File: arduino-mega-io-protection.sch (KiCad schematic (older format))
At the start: 34 parts, among them J108 CONN_01X36, J109 CONN_01X10, J110 CONN_02X18, J111 CONN_01X08, J112 CONN_01X08, J113 CONN_01X08, J114 CONN_01X08, J115 CONN_01X08

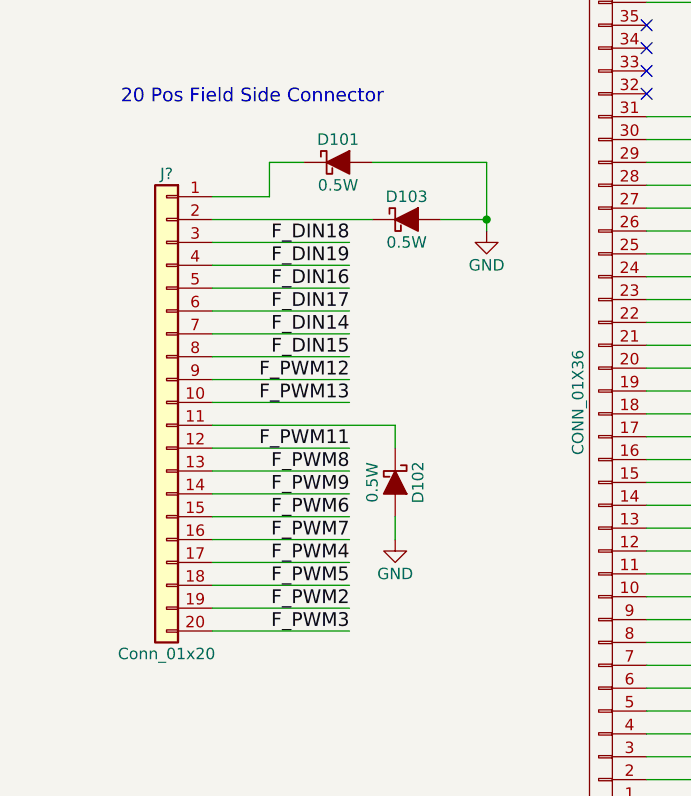
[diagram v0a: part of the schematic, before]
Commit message: updating schematic and library to use a Phoenix header for the 1x20
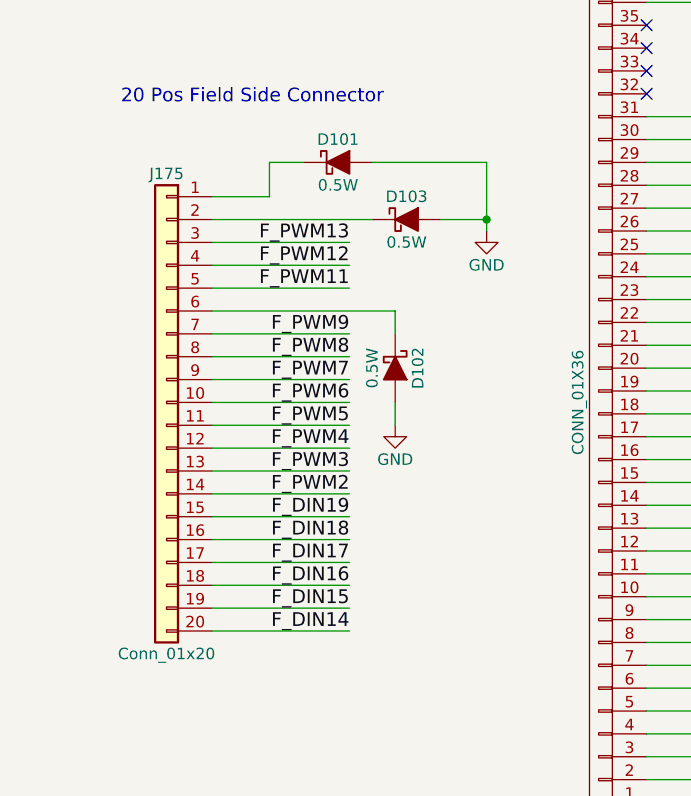
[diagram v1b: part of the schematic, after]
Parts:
- J175: renamed from J?; footprint (none) -> 3ML_Conn_Headers:Phoenix-1x20-1709678; MFN 1709678 -> Phoenix Contact
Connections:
- net F_DIN14: now also J175.20 (Pin_20); no longer J175.7 (Pin_7)
- net F_DIN15: now also J175.19 (Pin_19); no longer J175.8 (Pin_8)
- net F_DIN16: now also J175.18 (Pin_18); no longer J175.5 (Pin_5)
- net F_DIN17: now also J175.17 (Pin_17); no longer J175.6 (Pin_6)
- net F_DIN18: now also J175.16 (Pin_16); no longer J175.3 (Pin_3)
- net F_DIN19: now also J175.15 (Pin_15); no longer J175.4 (Pin_4)
- net F_PWM11: now also J175.5 (Pin_5); no longer J175.12 (Pin_12)
- net F_PWM12: now also J175.4 (Pin_4); no longer J175.9 (Pin_9)
- net F_PWM13: now also J175.3 (Pin_3); no longer J175.10 (Pin_10)
- net F_PWM2: now also J175.14 (Pin_14); no longer J175.19 (Pin_19)
- net F_PWM3: now also J175.13 (Pin_13); no longer J175.20 (Pin_20)
- net F_PWM4: now also J175.12 (Pin_12); no longer J175.17 (Pin_17)
- net F_PWM5: now also J175.11 (Pin_11); no longer J175.18 (Pin_18)
- net F_PWM6: now also J175.10 (Pin_10); no longer J175.15 (Pin_15)
- net F_PWM7: now also J175.9 (Pin_9); no longer J175.16 (Pin_16)
- net F_PWM8: now also J175.8 (Pin_8); no longer J175.13 (Pin_13)
- net F_PWM9: now also J175.7 (Pin_7); no longer J175.14 (Pin_14)
- net at D102.1 (K): now also J175.6 (Pin_6); no longer J175.11 (Pin_11)
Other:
- moved on the sheet: D102
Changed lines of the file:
@@
 Text Label 7800 2550 0    60   ~ 0
 F_PWM13
-Text Label 1950 5250 2    60   ~ 0
+Text Label 1950 4750 2    60   ~ 0
 F_PWM2
-Text Label 1950 5350 2    60   ~ 0
+Text Label 1950 4650 2    60   ~ 0
 F_PWM3
-Text Label 1950 5050 2    60   ~ 0
+Text Label 1950 4550 2    60   ~ 0
 F_PWM4
-Text Label 1950 5150 2    60   ~ 0
+Text Label 1950 4450 2    60   ~ 0
 F_PWM5
-Text Label 1950 4850 2    60   ~ 0
+Text Label 1950 4350 2    60   ~ 0
 F_PWM6
-Text Label 1950 4950 2    60   ~ 0
+Text Label 1950 4250 2    60   ~ 0
 F_PWM7
-Text Label 1950 4650 2    60   ~ 0
+Text Label 1950 4150 2    60   ~ 0
 F_PWM8
-Text Label 1950 4750 2    60   ~ 0
+Text Label 1950 4050 2    60   ~ 0
 F_PWM9
-Text Label 1950 4550 2    60   ~ 0
+Text Label 1950 3850 2    60   ~ 0
 F_PWM11
-Text Label 1950 4250 2    60   ~ 0
+Text Label 1950 3750 2    60   ~ 0
 F_PWM12
-Text Label 1950 4350 2    60   ~ 0
+Text Label 1950 3650 2    60   ~ 0
 F_PWM13
 $Comp
@@
 Text Label 11850 6250 0    60   ~ 0
 DIN19
-Text Label 1950 4050 2    60   ~ 0
+Text Label 1950 5350 2    60   ~ 0
 F_DIN14
-Text Label 1950 4150 2    60   ~ 0
+Text Label 1950 5250 2    60   ~ 0
 F_DIN15
-Text Label 1950 3850 2    60   ~ 0
+Text Label 1950 5150 2    60   ~ 0
 F_DIN16
-Text Label 1950 3950 2    60   ~ 0
+Text Label 1950 5050 2    60   ~ 0
 F_DIN17
-Text Label 1950 3650 2    60   ~ 0
+Text Label 1950 4950 2    60   ~ 0
 F_DIN18
-Text Label 1950 3750 2    60   ~ 0
+Text Label 1950 4850 2    60   ~ 0
 F_DIN19
 Text Label 7800 2400 0    60   ~ 0
@@
 L GND #PWR09
 U 1 1 593C6552
-P 2150 4950
-F 0 "#PWR09" H 2150 4700 50  0001 C CNN
-F 1 "GND" H 2150 4800 50  0000 C CNN
-F 2 "" H 2150 4950 50  0001 C CNN
-F 3 "" H 2150 4950 50  0001 C CNN
-	1    2150 4950
+P 2150 4450
+F 0 "#PWR09" H 2150 4200 50  0001 C CNN
+F 1 "GND" H 2150 4300 50  0000 C CNN
+F 2 "" H 2150 4450 50  0001 C CNN
+F 3 "" H 2150 4450 50  0001 C CNN
+	1    2150 4450
 	1    0    0    -1
 $EndComp
@@
 L D_Schottky_ALT D102
 U 1 1 598AE553
-P 2150 4700
-F 0 "D102" H 2150 4800 50  0000 C CNN
-F 1 "0.5W" H 2150 4600 50  0000 C CNN
-F 2 "Diodes_SMD:SOD-123" H 2150 4700 50  0001 C CNN
-F 3 "http://www.mccsemi.com/up_pdf/MBR0520~MBR0580(SOD123).pdf" H 2150 4700 50  0001 C CNN
-F 4 "X" H 2150 4700 60  0001 C CNN "Characteristics"
-F 5 "DIODE SCHOTTKY 80V 500MA SOD123" H 2150 4700 60  0001 C CNN "Description"
-F 6 "Micro Commercial Co" H 2150 4700 60  0001 C CNN "MFN"
-F 7 "SOD-123" H 2150 4700 60  0001 C CNN "Package ID"
-F 8 "Digikey" H 2150 4700 60  0001 C CNN "Source"
-F 9 "Y" H 2150 4700 60  0001 C CNN "Critical"
-F 10 "X" H 2150 4700 60  0001 C CNN "Notes"
-F 11 "1" H 2150 4700 60  0001 C CNN "Populate"
-F 12 "MBR0580-TP" H 2150 4700 60  0001 C CNN "MPN"
-	1    2150 4700
+P 2150 4200
+F 0 "D102" H 2150 4300 50  0000 C CNN
+F 1 "0.5W" H 2150 4100 50  0000 C CNN
+F 2 "Diodes_SMD:SOD-123" H 2150 4200 50  0001 C CNN
+F 3 "http://www.mccsemi.com/up_pdf/MBR0520~MBR0580(SOD123).pdf" H 2150 4200 50  0001 C CNN
+F 4 "X" H 2150 4200 60  0001 C CNN "Characteristics"
+F 5 "DIODE SCHOTTKY 80V 500MA SOD123" H 2150 4200 60  0001 C CNN "Description"
+F 6 "Micro Commercial Co" H 2150 4200 60  0001 C CNN "MFN"
+F 7 "SOD-123" H 2150 4200 60  0001 C CNN "Package ID"
+F 8 "Digikey" H 2150 4200 60  0001 C CNN "Source"
+F 9 "Y" H 2150 4200 60  0001 C CNN "Critical"
+F 10 "X" H 2150 4200 60  0001 C CNN "Notes"
+F 11 "1" H 2150 4200 60  0001 C CNN "Populate"
+F 12 "MBR0580-TP" H 2150 4200 60  0001 C CNN "MPN"
+	1    2150 4200
 	0    1    1    0
 $EndComp
@@
 20 Pos Field Side Connector
 $Comp
-L Conn_01x20 J?
+L Conn_01x20 J175
 U 1 1 59BED4D5
 P 1150 4350
-F 0 "J?" H 1150 5350 50  0000 C CNN
+F 0 "J175" H 1150 5350 50  0000 C CNN
 F 1 "Conn_01x20" H 1150 3250 50  0000 C CNN
-F 2 "" H 1150 4350 50  0001 C CNN
+F 2 "3ML_Conn_Headers:Phoenix-1x20-1709678" H 1150 4350 50  0001 C CNN
 F 3 "" H 1150 4350 50  0001 C CNN
 F 4 "Value" H 1150 4350 60  0001 C CNN "Characteristics"
@@
 F 10 "X" H 1150 4350 60  0001 C CNN "Notes"
 F 11 "1" H 1150 4350 60  0001 C CNN "Populate"
-F 12 "1709678" H 1150 4350 60  0001 C CNN "MFN"
 	1    1150 4350
 	-1   0    0    -1
@@
 	1350 4050 1950 4050
 Wire Wire Line
-	1350 3950 1950 3950
-Wire Wire Line
 	1350 3850 1950 3850
 Wire Wire Line
@@
 	5900 4800 5450 4800
 Wire Wire Line
-	1350 4450 2150 4450
+	1350 3950 2150 3950
 Wire Wire Line
 	14850 4050 15400 4050
@@
 	15400 4050 15400 3900
 Wire Wire Line
-	2150 4850 2150 4950
+	2150 4350 2150 4450
 Wire Wire Line
 	4150 2900 4150 3050
@@
 	2550 3550 2350 3550
 Wire Wire Line
-	2150 4450 2150 4550
+	2150 3950 2150 4050
 Wire Notes Line
 	500  7450 4900 7450
@@
 Text Notes 650  800  0    125  ~ 0
 Field Connections
+Wire Wire Line
+	1350 4450 1950 4450
 $EndSCHEMATC

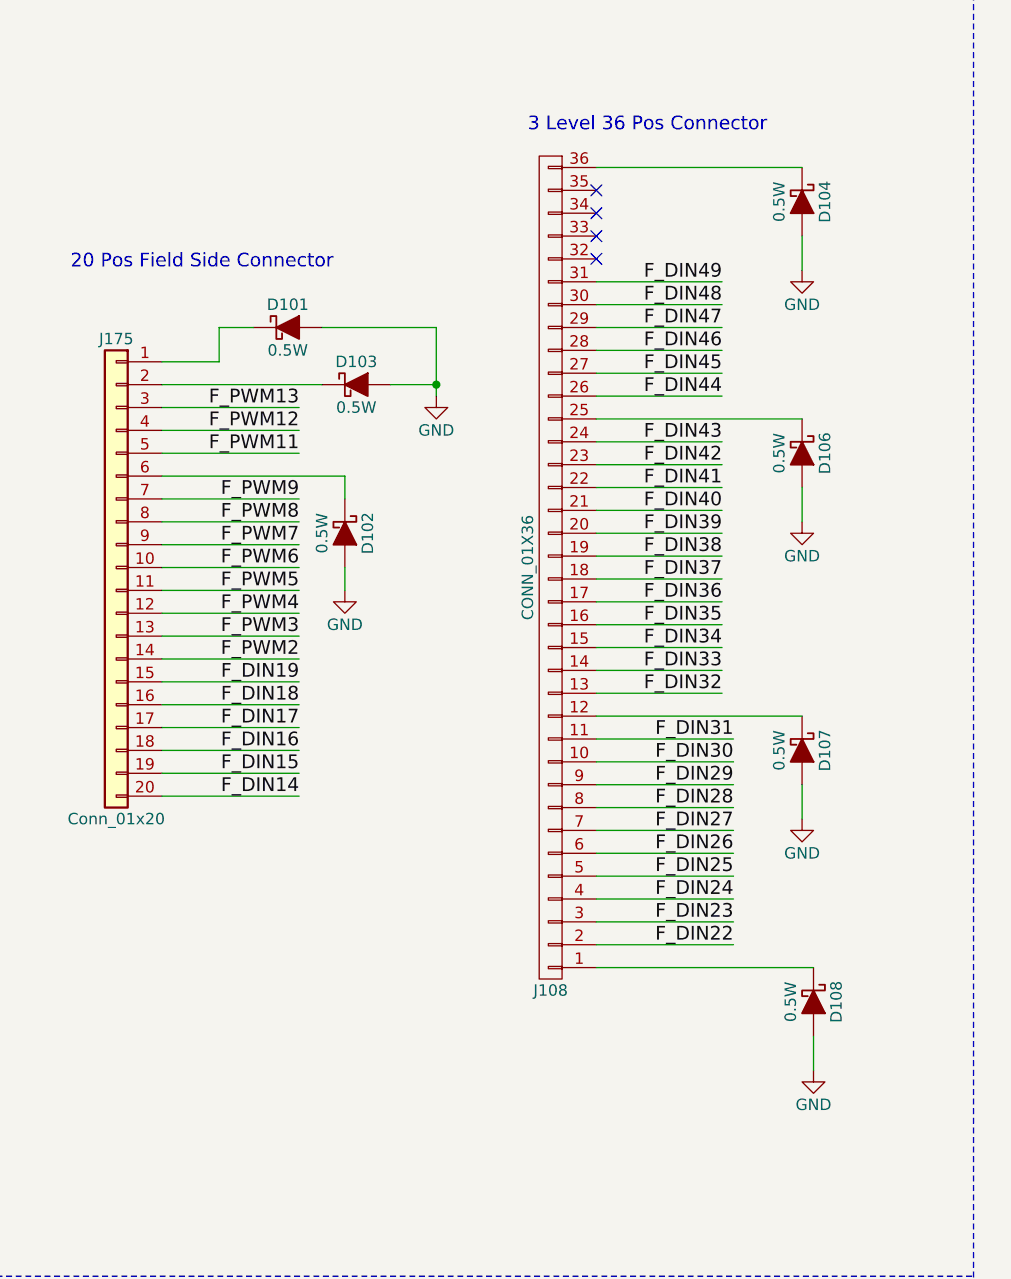
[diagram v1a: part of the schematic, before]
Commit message: removing unnecessary diodes
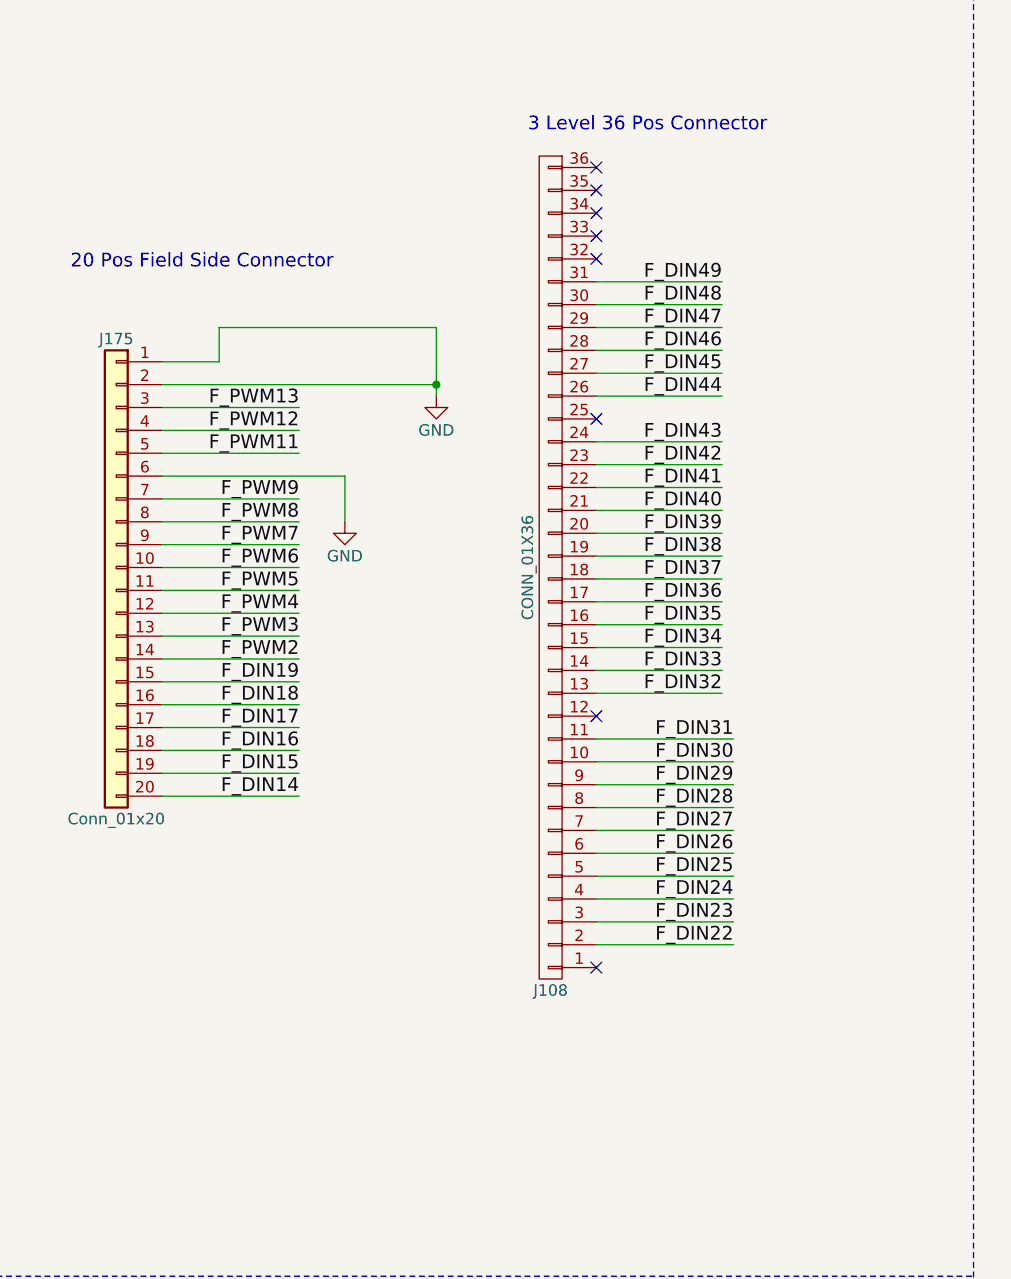
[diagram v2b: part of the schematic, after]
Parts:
- removed D101, D102, D103, D104, D106, D107, D108: 0.5W, Diodes_SMD:SOD-123, symbol D_Schottky_ALT
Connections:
- net GND: now also J175.1 (Pin_1), J175.2 (Pin_2), J175.6 (Pin_6)
- no-connect marks 33 -> 37
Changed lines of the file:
@@
 Text Notes 2950 2450 0    60   ~ 0
 3 Level 36 Pos Connector
-$Comp
-L GND #PWR07
-U 1 1 59059872
-P 4150 3050
-F 0 "#PWR07" H 4150 2800 50  0001 C CNN
-F 1 "GND" H 4150 2900 50  0000 C CNN
-F 2 "" H 4150 3050 50  0001 C CNN
-F 3 "" H 4150 3050 50  0001 C CNN
-	1    4150 3050
-	1    0    0    -1
-$EndComp
 Text Label 7800 4200 0    60   ~ 0
 F_PWM2
@@
 L GND #PWR09
 U 1 1 593C6552
-P 2150 4450
-F 0 "#PWR09" H 2150 4200 50  0001 C CNN
-F 1 "GND" H 2150 4300 50  0000 C CNN
-F 2 "" H 2150 4450 50  0001 C CNN
-F 3 "" H 2150 4450 50  0001 C CNN
-	1    2150 4450
+P 2150 4150
+F 0 "#PWR09" H 2150 3900 50  0001 C CNN
+F 1 "GND" H 2150 4000 50  0000 C CNN
+F 2 "" H 2150 4150 50  0001 C CNN
+F 3 "" H 2150 4150 50  0001 C CNN
+	1    2150 4150
 	1    0    0    -1
 $EndComp
@@
 $EndComp
 NoConn ~ 14850 4150
-$Comp
-L D_Schottky_ALT D103
-U 1 1 5989D79A
-P 2200 3550
-F 0 "D103" H 2200 3650 50  0000 C CNN
-F 1 "0.5W" H 2200 3450 50  0000 C CNN
-F 2 "Diodes_SMD:SOD-123" H 2200 3550 50  0001 C CNN
-F 3 "http://www.mccsemi.com/up_pdf/MBR0520~MBR0580(SOD123).pdf" H 2200 3550 50  0001 C CNN
-F 4 "X" H 2200 3550 60  0001 C CNN "Characteristics"
-F 5 "DIODE SCHOTTKY 80V 500MA SOD123" H 2200 3550 60  0001 C CNN "Description"
-F 6 "Micro Commercial Co" H 2200 3550 60  0001 C CNN "MFN"
-F 7 "SOD-123" H 2200 3550 60  0001 C CNN "Package ID"
-F 8 "Digikey" H 2200 3550 60  0001 C CNN "Source"
-F 9 "Y" H 2200 3550 60  0001 C CNN "Critical"
-F 10 "X" H 2200 3550 60  0001 C CNN "Notes"
-F 11 "1" H 2200 3550 60  0001 C CNN "Populate"
-F 12 "MBR0580-TP" H 2200 3550 60  0001 C CNN "MPN"
-	1    2200 3550
-	1    0    0    -1
-$EndComp
-$Comp
-L GND #PWR011
-U 1 1 598A7A47
-P 4150 4150
-F 0 "#PWR011" H 4150 3900 50  0001 C CNN
-F 1 "GND" H 4150 4000 50  0000 C CNN
-F 2 "" H 4150 4150 50  0001 C CNN
-F 3 "" H 4150 4150 50  0001 C CNN
-	1    4150 4150
-	1    0    0    -1
-$EndComp
-$Comp
-L GND #PWR012
-U 1 1 598AB066
-P 4150 5450
-F 0 "#PWR012" H 4150 5200 50  0001 C CNN
-F 1 "GND" H 4150 5300 50  0000 C CNN
-F 2 "" H 4150 5450 50  0001 C CNN
-F 3 "" H 4150 5450 50  0001 C CNN
-	1    4150 5450
-	1    0    0    -1
-$EndComp
-$Comp
-L GND #PWR013
-U 1 1 598AB93C
-P 4200 6550
-F 0 "#PWR013" H 4200 6300 50  0001 C CNN
-F 1 "GND" H 4200 6400 50  0000 C CNN
-F 2 "" H 4200 6550 50  0001 C CNN
-F 3 "" H 4200 6550 50  0001 C CNN
-	1    4200 6550
-	1    0    0    -1
-$EndComp
-$Comp
-L D_Schottky_ALT D101
-U 1 1 598ACBF0
-P 1900 3300
-F 0 "D101" H 1900 3400 50  0000 C CNN
-F 1 "0.5W" H 1900 3200 50  0000 C CNN
-F 2 "Diodes_SMD:SOD-123" H 1900 3300 50  0001 C CNN
-F 3 "http://www.mccsemi.com/up_pdf/MBR0520~MBR0580(SOD123).pdf" H 1900 3300 50  0001 C CNN
-F 4 "X" H 1900 3300 60  0001 C CNN "Characteristics"
-F 5 "DIODE SCHOTTKY 80V 500MA SOD123" H 1900 3300 60  0001 C CNN "Description"
-F 6 "Micro Commercial Co" H 1900 3300 60  0001 C CNN "MFN"
-F 7 "SOD-123" H 1900 3300 60  0001 C CNN "Package ID"
-F 8 "Digikey" H 1900 3300 60  0001 C CNN "Source"
-F 9 "Y" H 1900 3300 60  0001 C CNN "Critical"
-F 10 "X" H 1900 3300 60  0001 C CNN "Notes"
-F 11 "1" H 1900 3300 60  0001 C CNN "Populate"
-F 12 "MBR0580-TP" H 1900 3300 60  0001 C CNN "MPN"
-	1    1900 3300
-	1    0    0    -1
-$EndComp
-$Comp
-L D_Schottky_ALT D104
-U 1 1 598ACECD
-P 4150 2750
-F 0 "D104" H 4150 2850 50  0000 C CNN
-F 1 "0.5W" H 4150 2650 50  0000 C CNN
-F 2 "Diodes_SMD:SOD-123" H 4150 2750 50  0001 C CNN
-F 3 "http://www.mccsemi.com/up_pdf/MBR0520~MBR0580(SOD123).pdf" H 4150 2750 50  0001 C CNN
-F 4 "X" H 4150 2750 60  0001 C CNN "Characteristics"
-F 5 "DIODE SCHOTTKY 80V 500MA SOD123" H 4150 2750 60  0001 C CNN "Description"
-F 6 "Micro Commercial Co" H 4150 2750 60  0001 C CNN "MFN"
-F 7 "SOD-123" H 4150 2750 60  0001 C CNN "Package ID"
-F 8 "Digikey" H 4150 2750 60  0001 C CNN "Source"
-F 9 "Y" H 4150 2750 60  0001 C CNN "Critical"
-F 10 "X" H 4150 2750 60  0001 C CNN "Notes"
-F 11 "1" H 4150 2750 60  0001 C CNN "Populate"
-F 12 "MBR0580-TP" H 4150 2750 60  0001 C CNN "MPN"
-	1    4150 2750
-	0    1    1    0
-$EndComp
-$Comp
-L D_Schottky_ALT D106
-U 1 1 598AE26E
-P 4150 3850
-F 0 "D106" H 4150 3950 50  0000 C CNN
-F 1 "0.5W" H 4150 3750 50  0000 C CNN
-F 2 "Diodes_SMD:SOD-123" H 4150 3850 50  0001 C CNN
-F 3 "http://www.mccsemi.com/up_pdf/MBR0520~MBR0580(SOD123).pdf" H 4150 3850 50  0001 C CNN
-F 4 "X" H 4150 3850 60  0001 C CNN "Characteristics"
-F 5 "DIODE SCHOTTKY 80V 500MA SOD123" H 4150 3850 60  0001 C CNN "Description"
-F 6 "Micro Commercial Co" H 4150 3850 60  0001 C CNN "MFN"
-F 7 "SOD-123" H 4150 3850 60  0001 C CNN "Package ID"
-F 8 "Digikey" H 4150 3850 60  0001 C CNN "Source"
-F 9 "Y" H 4150 3850 60  0001 C CNN "Critical"
-F 10 "X" H 4150 3850 60  0001 C CNN "Notes"
-F 11 "1" H 4150 3850 60  0001 C CNN "Populate"
-F 12 "MBR0580-TP" H 4150 3850 60  0001 C CNN "MPN"
-	1    4150 3850
-	0    1    1    0
-$EndComp
-$Comp
-L D_Schottky_ALT D102
-U 1 1 598AE553
-P 2150 4200
-F 0 "D102" H 2150 4300 50  0000 C CNN
-F 1 "0.5W" H 2150 4100 50  0000 C CNN
-F 2 "Diodes_SMD:SOD-123" H 2150 4200 50  0001 C CNN
-F 3 "http://www.mccsemi.com/up_pdf/MBR0520~MBR0580(SOD123).pdf" H 2150 4200 50  0001 C CNN
-F 4 "X" H 2150 4200 60  0001 C CNN "Characteristics"
-F 5 "DIODE SCHOTTKY 80V 500MA SOD123" H 2150 4200 60  0001 C CNN "Description"
-F 6 "Micro Commercial Co" H 2150 4200 60  0001 C CNN "MFN"
-F 7 "SOD-123" H 2150 4200 60  0001 C CNN "Package ID"
-F 8 "Digikey" H 2150 4200 60  0001 C CNN "Source"
-F 9 "Y" H 2150 4200 60  0001 C CNN "Critical"
-F 10 "X" H 2150 4200 60  0001 C CNN "Notes"
-F 11 "1" H 2150 4200 60  0001 C CNN "Populate"
-F 12 "MBR0580-TP" H 2150 4200 60  0001 C CNN "MPN"
-	1    2150 4200
-	0    1    1    0
-$EndComp
-$Comp
-L D_Schottky_ALT D107
-U 1 1 598B1541
-P 4150 5150
-F 0 "D107" H 4150 5250 50  0000 C CNN
-F 1 "0.5W" H 4150 5050 50  0000 C CNN
-F 2 "Diodes_SMD:SOD-123" H 4150 5150 50  0001 C CNN
-F 3 "http://www.mccsemi.com/up_pdf/MBR0520~MBR0580(SOD123).pdf" H 4150 5150 50  0001 C CNN
-F 4 "X" H 4150 5150 60  0001 C CNN "Characteristics"
-F 5 "DIODE SCHOTTKY 80V 500MA SOD123" H 4150 5150 60  0001 C CNN "Description"
-F 6 "Micro Commercial Co" H 4150 5150 60  0001 C CNN "MFN"
-F 7 "SOD-123" H 4150 5150 60  0001 C CNN "Package ID"
-F 8 "Digikey" H 4150 5150 60  0001 C CNN "Source"
-F 9 "Y" H 4150 5150 60  0001 C CNN "Critical"
-F 10 "X" H 4150 5150 60  0001 C CNN "Notes"
-F 11 "1" H 4150 5150 60  0001 C CNN "Populate"
-F 12 "MBR0580-TP" H 4150 5150 60  0001 C CNN "MPN"
-	1    4150 5150
-	0    1    1    0
-$EndComp
-$Comp
-L D_Schottky_ALT D108
-U 1 1 598B1827
-P 4200 6250
-F 0 "D108" H 4200 6350 50  0000 C CNN
-F 1 "0.5W" H 4200 6150 50  0000 C CNN
-F 2 "Diodes_SMD:SOD-123" H 4200 6250 50  0001 C CNN
-F 3 "http://www.mccsemi.com/up_pdf/MBR0520~MBR0580(SOD123).pdf" H 4200 6250 50  0001 C CNN
-F 4 "X" H 4200 6250 60  0001 C CNN "Characteristics"
-F 5 "DIODE SCHOTTKY 80V 500MA SOD123" H 4200 6250 60  0001 C CNN "Description"
-F 6 "Micro Commercial Co" H 4200 6250 60  0001 C CNN "MFN"
-F 7 "SOD-123" H 4200 6250 60  0001 C CNN "Package ID"
-F 8 "Digikey" H 4200 6250 60  0001 C CNN "Source"
-F 9 "Y" H 4200 6250 60  0001 C CNN "Critical"
-F 10 "X" H 4200 6250 60  0001 C CNN "Notes"
-F 11 "1" H 4200 6250 60  0001 C CNN "Populate"
-F 12 "MBR0580-TP" H 4200 6250 60  0001 C CNN "MPN"
-	1    4200 6250
-	0    1    1    0
-$EndComp
 Text Notes 950  3050 0    60   ~ 0
 20 Pos Field Side Connector
@@
 	3250 3100 3800 3100
 Wire Wire Line
-	3250 2600 4150 2600
-Wire Wire Line
 	3250 3800 3800 3800
 Wire Wire Line
@@
 	15400 4050 15400 3900
 Wire Wire Line
-	2150 4350 2150 4450
-Wire Wire Line
-	4150 2900 4150 3050
-Wire Wire Line
-	3250 3700 4150 3700
-Wire Wire Line
-	4150 4000 4150 4150
-Wire Wire Line
-	3250 5000 4150 5000
-Wire Wire Line
-	4150 5300 4150 5450
-Wire Wire Line
-	3250 6100 4200 6100
-Wire Wire Line
-	4200 6400 4200 6550
+	2150 3950 2150 4150
 Wire Wire Line
 	1350 3450 1600 3450
@@
 	1600 3450 1600 3300
 Wire Wire Line
-	1600 3300 1750 3300
-Wire Wire Line
-	1350 3550 2050 3550
+	1600 3300 2550 3300
+Wire Wire Line
+	1350 3550 2550 3550
 Wire Wire Line
 	2550 3300 2550 3600
-Wire Wire Line
-	2050 3300 2550 3300
 Connection ~ 2550 3550
-Wire Wire Line
-	2550 3550 2350 3550
-Wire Wire Line
-	2150 3950 2150 4050
 Wire Notes Line
 	500  7450 4900 7450
@@
 Wire Wire Line
 	1350 4450 1950 4450
+NoConn ~ 3250 5000
+NoConn ~ 3250 6100
+NoConn ~ 3250 3700
+NoConn ~ 3250 2600
 $EndSCHEMATC
